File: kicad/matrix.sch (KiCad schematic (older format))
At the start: 30 parts, among them Q1 Q_NMOS_DGS

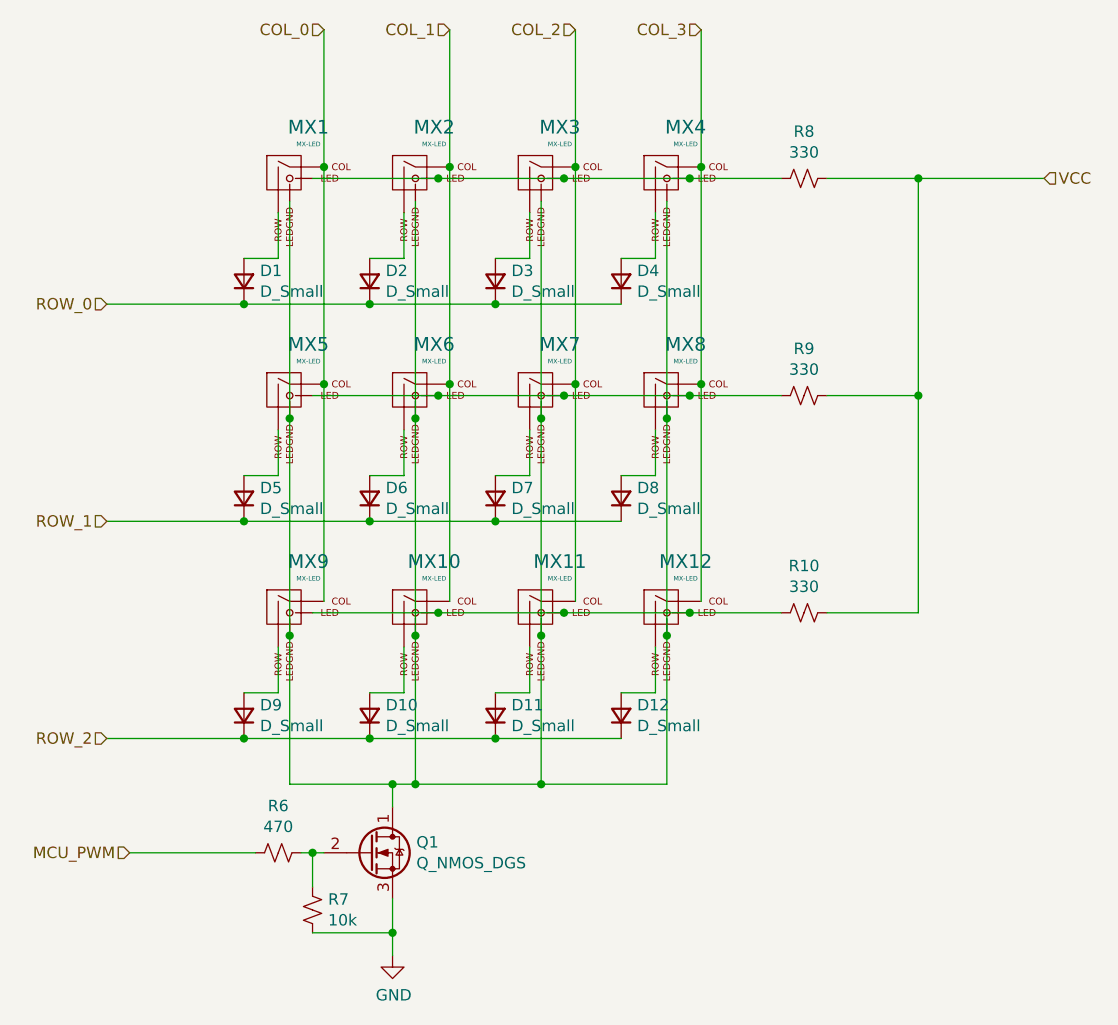
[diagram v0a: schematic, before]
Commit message: Adds kicad directory for kicad stuff
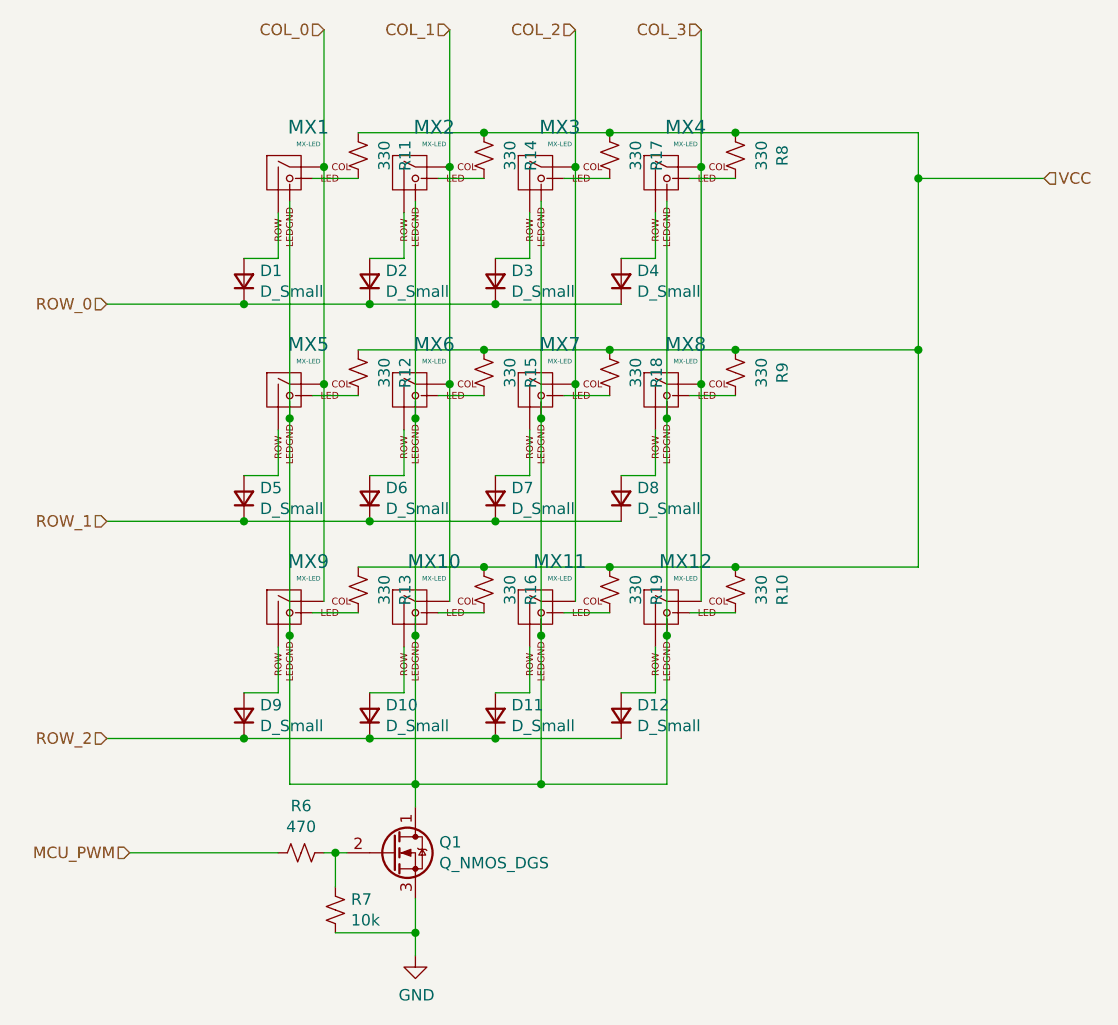
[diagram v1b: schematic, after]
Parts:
- added R11, R12, R13, R14, R15, R16, R17, R18, R19: 330, Resistor_SMD:R_0805_2012Metric, symbol Device:R_Small_US
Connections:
- net VCC: now also R10.2, R8.2, R9.2, R11.2, R12.2, R13.2, R14.2, R15.2, R16.2, R17.2, R18.2, R19.2; no longer R10.1, R8.1, R9.1
- new net: MX12.3 (LED), R10.1
- new net: MX11.3 (LED), R19.1
- new net: MX10.3 (LED), R16.1
- new net: MX9.3 (LED), R13.1
- new net: MX8.3 (LED), R9.1
- new net: MX7.3 (LED), R18.1
- new net: MX4.3 (LED), R8.1
- new net: MX3.3 (LED), R17.1
- new net: MX6.3 (LED), R15.1
- new net: MX5.3 (LED), R12.1
- new net: MX2.3 (LED), R14.1
- new net: MX1.3 (LED), R11.1
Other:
- moved on the sheet: Q1, R10, R6, R7, R8, R9

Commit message: Adds iBom and final revision of board
Puts holes in the right place for the case
Adds proper backlight support with a properly sized mosfet (tiny)
Double checks dimensions
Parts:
- removed Q1: Q_NMOS_DGS, Package_TO_SOT_SMD:SOT-723, symbol Device:Q_NMOS_DGS
- added Q1: Q_NMOS_GDS, Package_TO_SOT_SMD:SOT-23, symbol Device:Q_NMOS_GDS
- R6: value 470 -> 20k
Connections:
- net GND: now also Q1.3 (S)
- net at MX1.4 (LEDGND), MX10.4 (LEDGND), MX11.4 (LEDGND)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: now also Q1.2 (D)
- net at R6.1, R7.1: now also Q1.1 (G)
